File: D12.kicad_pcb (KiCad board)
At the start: 4 copper layers, 50.9 x 15.5 mm, 72 parts, among them IC1 DRV8847RTER, IC2 NCP730BM, J1 Conn_01x01, J2 Conn_01x01, J3 Conn_01x01, J4 Conn_01x01, J5 Conn_01x01, J6 Conn_01x01, J7 UDPI, J8 Conn_01x01, J9 Conn_01x01, Q1 BC857BDW1, Q2 BC847BDW1, U1 AVR-64DA32, U2 BNO055, U4 TPS22810DRVR

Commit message: initial
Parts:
- removed C10: 1u, Capacitor_SMD:C_0402_1005Metric
- removed C14: 220uF, Capacitor_SMD:C_1206_3216Metric
- removed C17: 100u/16V, Capacitor_SMD:C_1210_3225Metric
- removed C18: 47uF, Capacitor_SMD:C_0603_1608Metric
- removed C5, C6: 100u/16V, Capacitor_SMD:C_1206_3216Metric
- removed C7: N x 47u/25V, Capacitor_SMD:C_1206_3216Metric
- removed C8, C9: 100n, Capacitor_SMD:C_0402_1005Metric
- removed D1, D9: CDBURT0530, Diode_SMD:D_0603_1608Metric
- removed R14, R17: 10k, Resistor_SMD:R_0402_1005Metric
- removed R16: 200, Resistor_SMD:R_0805_2012Metric
- removed R8: n.f., Resistor_SMD:R_0402_1005Metric
- removed U2: BNO055, Package_LGA:LGA-28_5.2x3.8mm_P0.5mm
- added J10: Motor 1, RTB:DummyNet-Connector, F.Cu at (66.0, -50.2)
- added J11: Motor 2, RTB:DummyNet-Connector, F.Cu at (65.9, -36.3)
- added J12: Vtrk, RTB:DummyNet-Connector, F.Cu at (88.9, -47.5)
- added J13: AUX4.od, RTB:DummyNet-Connector, F.Cu at (90.7, -47.4)
- added J14: Vtrk, RTB:DummyNet-Connector, F.Cu at (88.9, -39.0)
- added J15: AUX3.od, RTB:DummyNet-Connector, F.Cu at (90.7, -39.0)
- added J16: Aux1, RTB:DummyNet-Connector, F.Cu at (49.2, -42.3)
- added J17: Aux2, RTB:DummyNet-Connector, F.Cu at (97.2, -42.4)
- added J18: Conn_01x01, RTB:DummyNet-Connector, F.Cu at (97.2, -44.2)
- added J19: Conn_01x01, RTB:DummyNet-Connector, F.Cu at (49.2, -44.1)
- added J20: Conn_01x01, TestPoint:TestPoint_Pad_1.0x1.0mm, F.Cu at (95.7, -43.3)
- added J21: Conn_01x01, TestPoint:TestPoint_Pad_1.0x1.0mm, F.Cu at (50.7, -43.2)
- added Q3: PMZB200UNEYL, RTB:PMZB200UNEYL, F.Cu at (89.8, -41.0)
- added Q4: PMZB200UNEYL, RTB:PMZB200UNEYL, F.Cu at (89.8, -45.6)
- C1: value 4.7u/25V -> 100n/50V; footprint Capacitor_SMD:C_0603_1608Metric -> Capacitor_SMD:C_0402_1005Metric; moved to B.Cu
- C12: value 47uF -> 100u/4V; footprint Capacitor_SMD:C_0603_1608Metric -> Capacitor_SMD:C_0805_2012Metric; moved to B.Cu
- C2, C3: value 100u/16V -> 330u/20V; footprint Capacitor_SMD:C_1206_3216Metric -> Capacitor_Tantalum_SMD:CP_EIA-7361-38_AVX-V
- C22: value 1u/25V -> 1u
- C4: value 100u/16V -> 100n; footprint Capacitor_SMD:C_1206_3216Metric -> Capacitor_SMD:C_0402_1005Metric
- D2: value CDBURT0530 -> SM5819L2-TP; footprint Diode_SMD:D_0603_1608Metric -> RTB:SM5819L2TP
- D3: footprint LED_SMD:LED_0603_1608Metric -> LED_SMD:LED_0402_1005Metric
- D4, D7, D8: value D -> SM5819L2-TP; footprint Diode_SMD:D_0603_1608Metric -> RTB:SM5819L2TP
- D5: value LED(ylw) -> LED(pnk)
- IC1: value DRV8847RTER -> DRV8231ADSGR; footprint RTB:QFN50P300X300X80-17N-D -> RTB:SON50P200X200X80-9N; moved to B.Cu
- J7: footprint Connector_PinHeader_1.27mm:PinHeader_2x04_P1.27mm_Vertical -> RTB:DummyNet-Connector; moved to F.Cu
- R1: value 10k -> 3.3k
- R10, R12: value 68k -> 33k
- R11, R13: value 10k -> 12k
- R2: value 0.3 -> 2.2k; footprint Resistor_SMD:R_0805_2012Metric -> Resistor_SMD:R_0402_1005Metric
- R4: value n.f. -> 2.2k
- R5: value 10k -> 220k
- R7: value 10k -> 1; footprint Resistor_SMD:R_0402_1005Metric -> Resistor_SMD:R_0603_1608Metric; moved to B.Cu
- moved R1 38.2 mm to (57.6, -47.3), turned to 270 degrees
- moved R24 35.5 mm to (62.3, -46.6), turned to 90 degrees
- moved R4 33.5 mm to (61.9, -45.2), turned to 0 degrees
- moved R22 21.9 mm to (73.1, -43.3), turned to 90 degrees
- moved IC2 21.2 mm to (60.9, -43.2), turned to 90 degrees
- moved J7 15.5 mm to (75.4, -39.4)
- moved IC1 13.1 mm to (54.9, -43.2), turned to 270 degrees
- moved R2 11.9 mm to (60.0, -45.1), turned to 180 degrees
- moved R25 10.6 mm to (58.5, -47.3), turned to 270 degrees
- moved C2 9.60 mm to (67.3, -46.9), turned to 0 degrees
- moved C3 9.56 mm to (67.3, -39.7), turned to 0 degrees
- moved C1 8.41 mm to (56.7, -43.2), turned to 90 degrees
- moved R5 8.33 mm to (87.5, -41.7), turned to 0 degrees
- moved C12 8.09 mm to (93.0, -43.3), turned to 180 degrees
- moved C4 7.78 mm to (62.6, -43.3), turned to 270 degrees
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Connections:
- C20 pad 1: Net-(C20-Pad1) -> VTRK
- C3 pad 1: Net-(C3-Pad1) -> VHBR
- C4 pad 1: Net-(C3-Pad1) -> VHBR
- D5 pad 2: +3V3 -> LED.hbt
- IC1 pad 1: GND -> Net-(IC1-Pad1)
- IC1 pad 2: (no net) -> PWM2
- IC1 pad 3: M2 -> PWM1
- IC1 pad 4: Net-(IC1-Pad4) -> Vref
- IC1 pad 5: M1 -> VHBR
- IC1 pad 6: ~FAULT -> M1
- IC1 pad 7: PWM1 -> GND
- IC1 pad 8: PWM2 -> M2
- IC1 pad 9: TRQ -> GND
- IC2 pad 6: Net-(C3-Pad1) -> VHBR
- J7 pad 1: V24.rts -> UPDI
- R1 pad 2: Net-(R1-Pad2) -> Net-(IC1-Pad1)
- R2 pad 1: Net-(IC1-Pad4) -> AUX1
- R2 pad 2: GND -> Net-(J16-Pad1)
- R23 pad 1: LED.hbt -> Net-(D5-Pad1)
- R23 pad 2: Net-(D5-Pad1) -> GND
- R4 pad 1: GND -> AUX2
- R4 pad 2: Net-(R4-Pad2) -> Net-(J17-Pad1)
- R5 pad 1: Net-(R5-Pad1) -> iSENSa
- R5 pad 2: +3V3 -> Net-(Q3-Pad2)
- R7 pad 1: Net-(R4-Pad2) -> GND
- R7 pad 2: +3V3 -> Net-(Q3-Pad2)
- R9 pad 1: Net-(IC1-Pad4) -> ISENS
- R9 pad 2: ISENS -> Net-(IC1-Pad1)
- U1 pad 1: TRQ -> LED.rear
- U1 pad 13: LED.rear -> (no net)
- U1 pad 14: LED.fs1 -> iSENSa
- U1 pad 15: LED.front -> uSENS2
- U1 pad 16: (no net) -> Vref
- U1 pad 17: uSENS2 -> UDCC-b
- U1 pad 2: PWM2 -> PWM1
- U1 pad 20: UDCC-b -> Net-(R6-Pad2)
- U1 pad 21: ACK -> AUX3
- U1 pad 22: (no net) -> AUX4
- U1 pad 23: Net-(R6-Pad2) -> LED.fs1
- U1 pad 25: V24.rts -> LED.hbt
- U1 pad 26: V24.cts -> (no net)
- U1 pad 3: PWM1 -> PWM2
- U1 pad 30: V24.tx -> AUX1
- U1 pad 31: V24.rx -> AUX2
- U1 pad 32: LED.hbt -> LED.front
- U1 pad 4: ~FAULT -> (no net)
- U1 pad 5: BNO.res -> (no net)
- U1 pad 6: BNO.tx -> (no net)
- U1 pad 7: BNO.rx -> (no net)
- U1 pad 9: UDCC-a -> (no net)
- U4 pad 5: Net-(C20-Pad1) -> VTRK
- U4 pad 6: Net-(C20-Pad1) -> VTRK
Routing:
- net AUX4: track 0.00 -> 60.5 mm, vias 0 -> 3
- net LED.front: track 60.2 -> 4.97 mm, vias 2 -> 0
- net Net-(J17-Pad1): track 0.00 -> 53.4 mm, vias 0 -> 2
- net AUX3: track 0.00 -> 50.7 mm, vias 0 -> 2
- net Net-(J1-Pad1): track 0.00 -> 48.3 mm, vias 1 -> 2
- net BNO.res: track 47.1 -> 0.00 mm, vias 3 -> 0
- net iSENSa: track 0.00 -> 38.5 mm, vias 0 -> 3
- net BNO.tx: track 38.1 -> 0.00 mm, vias 3 -> 0
- net BNO.rx: track 37.8 -> 0.00 mm, vias 1 -> 0
- net Net-(C3-Pad1): track 35.4 -> 0.00 mm, vias 2 -> 0
- net GND: track 60.8 -> 25.8 mm, vias 32 -> 20
- net Net-(D3-Pad1): track 29.9 -> 0.97 mm, vias 2 -> 0
- net UPDI: track 1.94 -> 26.6 mm, vias 1 -> 2
- net Net-(IC1-Pad4): track 16.5 -> 0.00 mm, vias 2 -> 0
- net ACK: track 16.4 -> 0.00 mm, vias 3 -> 0
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- removed copper zone on B.Cu, net +3V3
- removed copper zone on F.Cu, net M1
- removed copper zone on F.Cu, net M2
- removed copper zone on B.Cu, net Net-(J1-Pad1)
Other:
- rule pad_to_mask_clearance: 0.2 -> 0
- rule trace_min: 0.15 -> 0.09
- rule via_min_drill: 0.2 -> 0.3
- rule via_min_size: 0.4 -> 0.45
- board text added: "+"
- board text added: "Aux3"
- board text added: "Aux4"
- board text added: "D12.5"
- board text added: "FS 2024"
- board text added: "r"
- board text added: "w"
- board text removed: "D12.4"
- board text removed: "FS 2022"

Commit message: mod: led automation
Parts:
- removed C16: 100nF, Capacitor_SMD:C_0402_1005Metric
- removed C20: 100n/50V, Capacitor_SMD:C_0402_1005Metric
- removed U4: TPS22810DRVR, Package_DFN_QFN:DFN-6-1EP_2x2mm_P0.65mm_EP1x1.6mm
- added C5: 100n, Capacitor_SMD:C_0402_1005Metric, F.Cu at (51.9, -41.1)
- added D1: SM5819L2-TP, RTB:SM5819L2TP, F.Cu at (87.5, -40.7)
- added D6: SM5819L2-TP, RTB:SM5819L2TP, F.Cu at (87.5, -44.9)
- added D9: SM5819L2-TP, RTB:SM5819L2TP, F.Cu at (74.2, -43.3)
- added R8: 68, Resistor_SMD:R_0402_1005Metric, F.Cu at (75.2, -43.3)
- C1: value 100n/50V -> 2.2u/35V
- C4: value 100n -> 4.7u/25V
- J10: value Motor 1 -> Motor A
- J11: value Motor 2 -> Motor B
- R1: value 3.3k -> 1k
- moved R3 3.50 mm to (83.2, -43.3)
- moved Q1 3.35 mm to (81.5, -43.3)
- moved Q2 3.35 mm to (78.3, -43.3)
- moved R15 3.35 mm to (79.9, -42.4)
- moved R18 3.35 mm to (79.9, -44.2)
- moved J7 0.05 mm to (75.5, -39.5)
- turned C2 to 180 degrees
- turned C3 to 180 degrees
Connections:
- net ISENS renamed iSENSm
- net LED.fs1 renamed LED.cab
- C2 pad 1: VHBR -> Net-(C2-Pad1)
- C3 pad 1: VHBR -> Net-(C2-Pad1)
- D4 pad 1: VTRK -> VHBR
- D7 pad 1: VTRK -> VHBR
- J12 pad 1: VTRK -> VHBR
- J14 pad 1: VTRK -> VHBR
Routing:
- net VHBR: track 42.0 -> 65.7 mm, vias 1 -> 6
- net VTRK: track 19.8 -> 0.00 mm, vias 3 -> 0
- net Net-(C2-Pad1): track 0.00 -> 13.1 mm, vias 0 -> 2
- net RCM.tx: track 20.4 -> 23.7 mm
- net DCC-b: track 51.5 -> 48.1 mm
- net GND: track 25.8 -> 22.5 mm, vias 20 -> 18
- net DCC-a: track 54.2 -> 51.3 mm
- net P2: track 2.29 -> 5.09 mm
- net P1: track 2.32 -> 4.27 mm
- net Net-(C16-Pad1): track 1.27 -> 0.00 mm
- net iSENSa: track 38.5 -> 37.8 mm
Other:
- board text added: "D12.6"
- board text added: "FS 2025"
- board text removed: "D12.5"
- board text removed: "FS 2024"

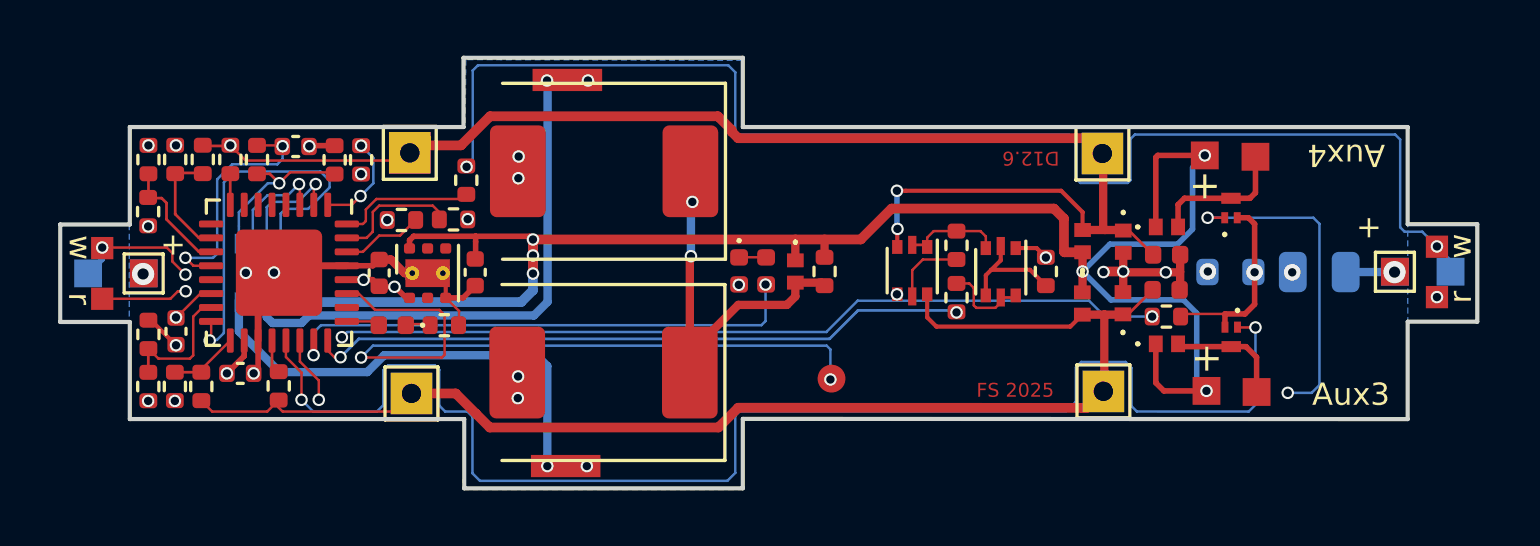
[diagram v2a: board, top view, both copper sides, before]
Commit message: migrated to Kicad 10
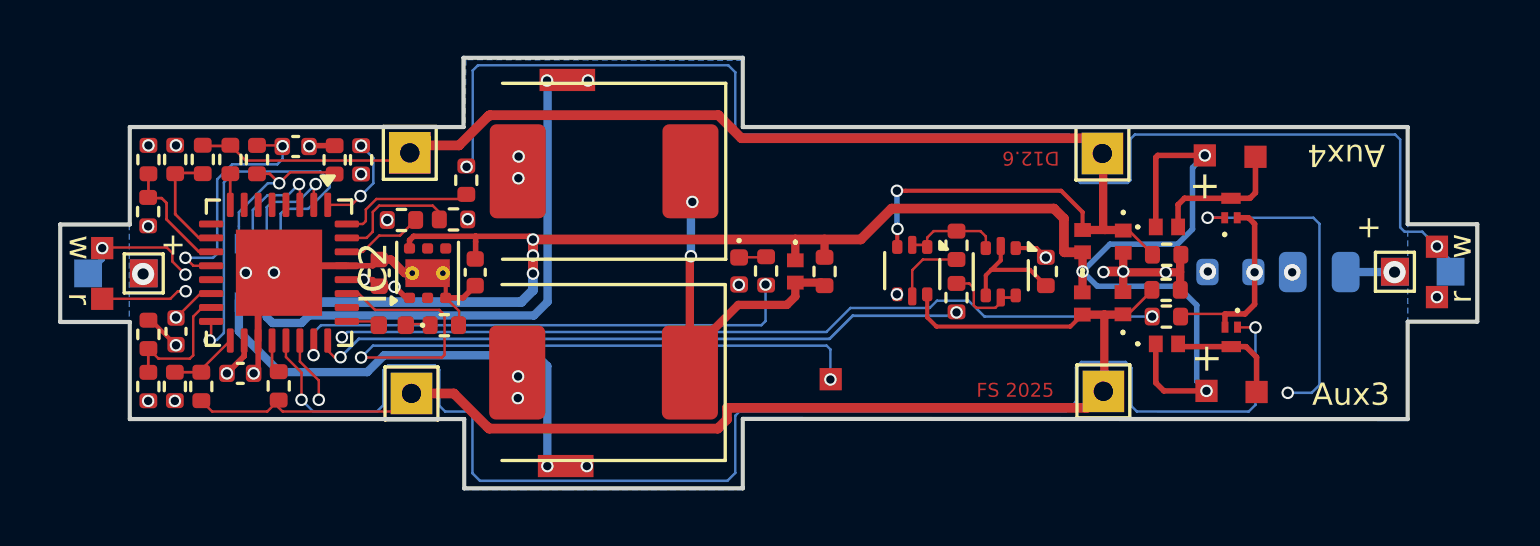
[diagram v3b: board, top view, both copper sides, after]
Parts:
- C1: value 2.2u/35V -> 100n/50V
- C11, C13: value 1u -> 10u/6.3V
- C12: value 100u/4V -> 47uF/6.3V
- D3: value LED(ylw) -> LED
- D5: value LED(pnk) -> LED
- IC2: value NCP730BM -> NCP730BMT500TBG
- J10, J11: footprint RTB:DummyNet-Connector -> RTB:Solder 2.0 x 0.8
- J12, J13, J14, J15, J16, J17, J18, J19, J7: footprint RTB:DummyNet-Connector -> RTB:Solder 0.8 x 0.8
- R5: value 220k -> 33k
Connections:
- IC2 pad 2: (no net) -> unconnected-(IC2-NC/ADJ-Pad2)
- IC2 pad 4: (no net) -> unconnected-(IC2-EN-Pad4)
- IC2 pad 5: (no net) -> unconnected-(IC2-NC/PG-Pad5)
- U1 pad 13: (no net) -> unconnected-(U1-PD3-Pad13)
- U1 pad 26: (no net) -> unconnected-(U1-PF6/~{RESET}-Pad26)
- U1 pad 4: (no net) -> unconnected-(U1-PA6-Pad4)
- U1 pad 5: (no net) -> unconnected-(U1-PA7-Pad5)
- U1 pad 6: (no net) -> unconnected-(U1-PC0-Pad6)
- U1 pad 7: (no net) -> unconnected-(U1-PC1-Pad7)
- U1 pad 9: (no net) -> unconnected-(U1-PC3-Pad9)
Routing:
- net DCC-a: vias 3 -> 2
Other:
- net class Default removed
- net class Power removed
